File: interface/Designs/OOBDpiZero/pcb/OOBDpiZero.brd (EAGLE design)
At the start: 73.5 x 42 mm, 132 parts, among them IC1 EEPROM24, IC100 LM1117MPX-3.3, IC2 DS3231, Q1 12MHz, U1 MAX98357, U100 SY6280, U101 SN65HVD230(SO8), U102 SN65HVD230(SO8), U2 MP1482

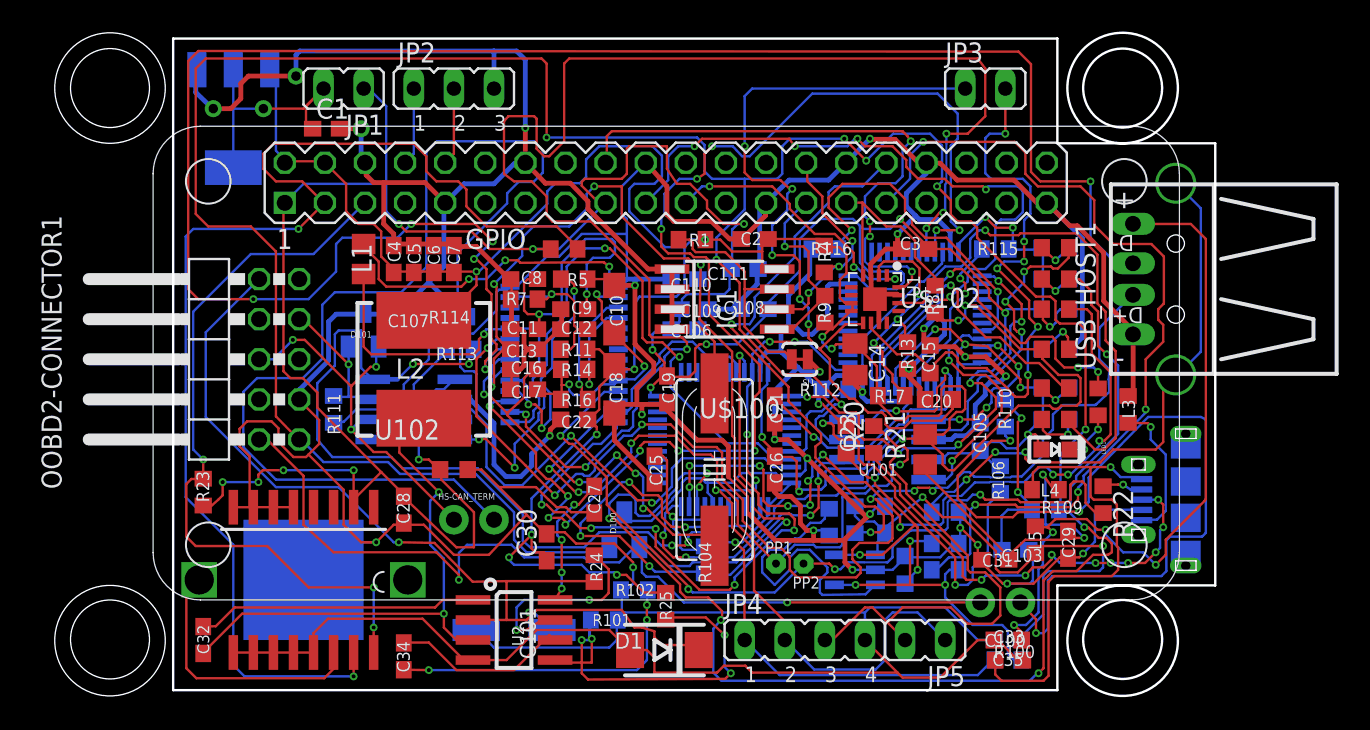
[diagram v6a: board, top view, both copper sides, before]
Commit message: all GND wires set to 12mil !!!optimization ongoing!!! next steps would be 3V3, 5V and planes
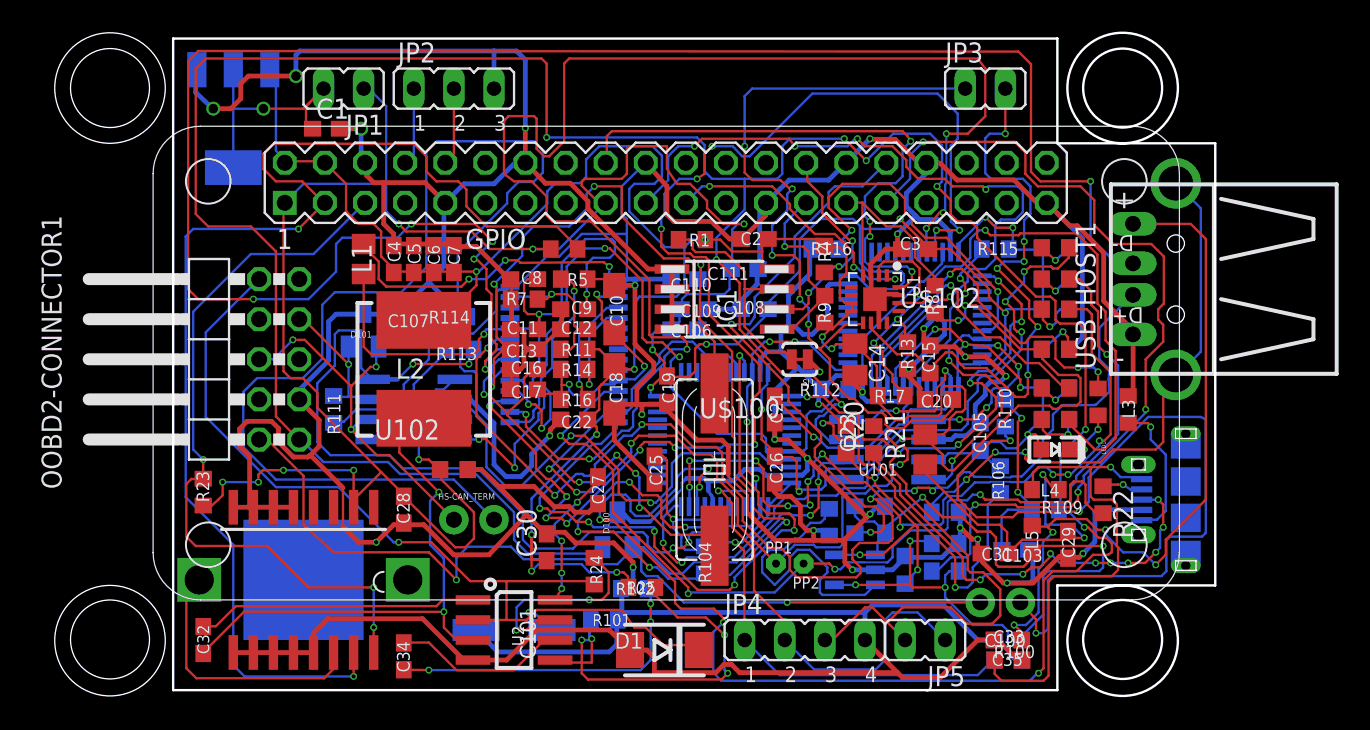
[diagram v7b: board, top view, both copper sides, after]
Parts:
- moved R25 1.92 mm to (29.7, 5.87), turned to 180 degrees
- moved C27 0.64 mm to (26.9, 12.0)
- moved D100 0.44 mm to (28.1, 9.53)
- moved C31 0.40 mm to (52.0, 8.02)
- moved L5 0.20 mm to (54.4, 8.93)
- moved R24 0.16 mm to (26.7, 6.91)
- moved R103 0.08 mm to (48.9, 6.91)
- moved R102 0.08 mm to (29.2, 5.79)
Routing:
- net +5V: track 189.4 -> 186.2 mm
- net GND: track 594.7 -> 597.2 mm
- net N$13: track 79.9 -> 82.0 mm
- net N$62: track 25.8 -> 27.3 mm
- net HS-CAN_TXD: track 34.4 -> 35.8 mm
- net N$5: track 54.6 -> 55.3 mm
- net N$4: track 8.51 -> 9.22 mm
- net +3V3: track 290.9 -> 290.3 mm
- net N$1: track 21.5 -> 22.1 mm
- net PP23: track 51.5 -> 52.1 mm
- net N$20: track 49.3 -> 49.9 mm
- net N$14: track 50.3 -> 50.9 mm

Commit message: commit before creating GND plane
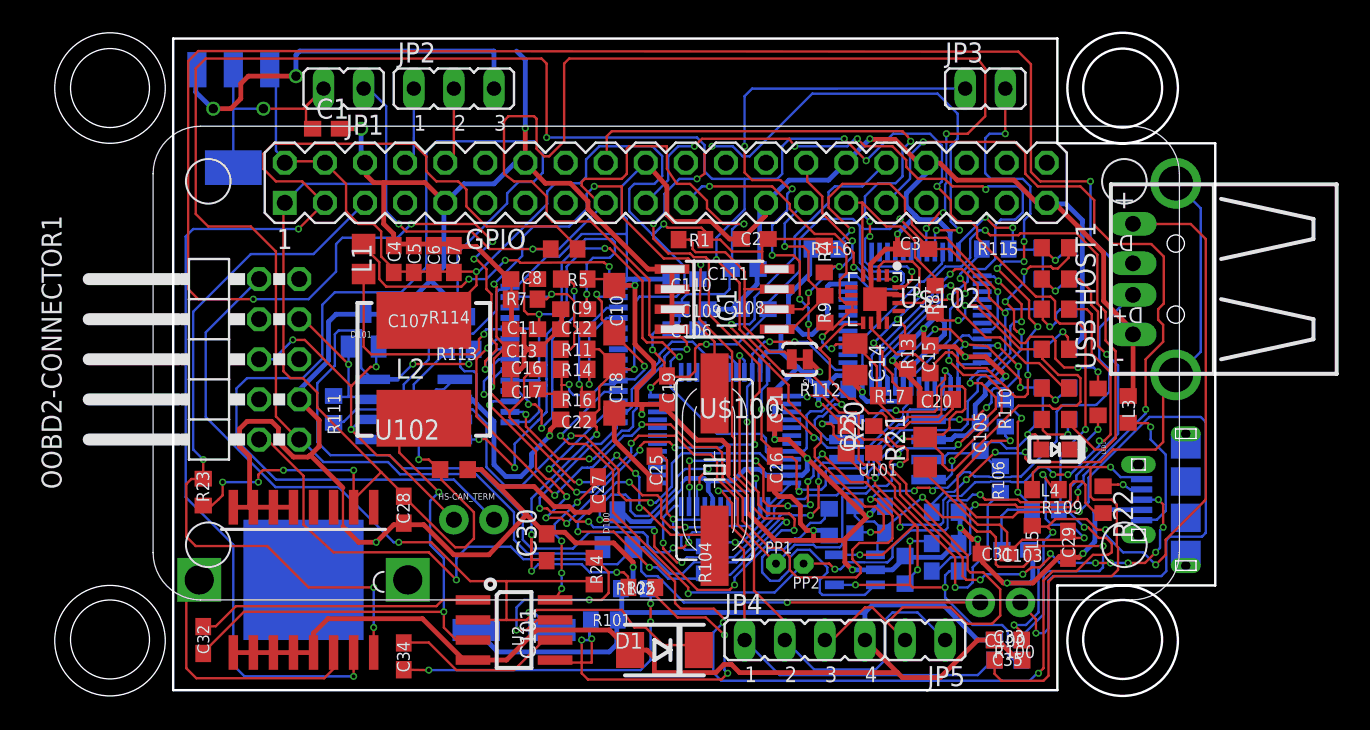
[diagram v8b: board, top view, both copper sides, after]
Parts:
- moved R21 0.16 mm to (47.6, 14.4)
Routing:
- net GND: track 597.2 -> 601.0 mm
- net +5V: track 186.2 -> 188.4 mm
- net N$39: track 46.7 -> 48.0 mm
- net N$30: track 67.2 -> 68.0 mm
- net HS-CAN_RXD: track 44.2 -> 43.6 mm
- net N$40: track 15.3 -> 14.8 mm
